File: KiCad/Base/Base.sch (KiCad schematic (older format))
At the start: 27 parts

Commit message: Base board draft 1
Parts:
- removed J?: Conn_01x02_Male, symbol Connector:Conn_01x02_Male
- removed Q?: IRF540N, Package_TO_SOT_THT:TO-220-3_Vertical, symbol Transistor_FET:IRF540N
- removed SW?: Power, symbol Switch:SW_SPDT
- removed U?: 4050, symbol 4xxx:4050
- removed U?: SHT1x, symbol Sensor:SHT1x
- added J14: Power_switch, Connector_PinHeader_2.54mm:PinHeader_1x02_P2.54mm_Vertical, symbol Connector:Conn_01x02_Male
- added J15: VCC, Connector_PinHeader_2.54mm:PinHeader_1x10_P2.54mm_Vertical, symbol Connector:Conn_01x10_Male
- added J16: GND, Connector_PinHeader_2.54mm:PinHeader_1x10_P2.54mm_Vertical, symbol Connector:Conn_01x10_Male
- J1: renamed from J?; footprint (none) -> Connector_PinHeader_2.54mm:PinHeader_2x20_P2.54mm_Vertical
- J10: renamed from J?; value Conn_01x02_Male -> MOSFET_output_1; footprint (none) -> Connector_PinHeader_2.54mm:PinHeader_1x02_P2.54mm_Vertical
- J11: renamed from J?; value Conn_01x02_Male -> MOSFET_output_2; footprint (none) -> Connector_PinHeader_2.54mm:PinHeader_1x02_P2.54mm_Vertical
- J12: renamed from J?; value Conn_01x02_Male -> MOSFET_output_3; footprint (none) -> Connector_PinHeader_2.54mm:PinHeader_1x02_P2.54mm_Vertical
- J2, J3: renamed from J?; footprint (none) -> Connector_PinHeader_2.54mm:PinHeader_1x10_P2.54mm_Vertical
- J4: renamed from J?; footprint (none) -> Connector_BarrelJack:BarrelJack_Horizontal
- J5: renamed from J?; footprint (none) -> Connector_PinHeader_2.54mm:PinHeader_1x04_P2.54mm_Vertical
- J6, J7, J8: renamed from J?; footprint (none) -> Connector_PinHeader_2.54mm:PinHeader_1x14_P2.54mm_Vertical
- J9: renamed from J?; value Conn_01x02_Male -> MOSFET_output_0; footprint (none) -> Connector_PinHeader_2.54mm:PinHeader_1x02_P2.54mm_Vertical
- R1, R2: renamed from R?; footprint (none) -> Resistor_THT:R_Axial_DIN0207_L6.3mm_D2.5mm_P10.16mm_Horizontal
- U1: renamed from U?; footprint (none) -> Package_DIP:DIP-16_W7.62mm_Socket
- gave numbers to parts that had none: 4
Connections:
- net labels added: PWM0
- net labels removed: GPC6, GPC7, GPC8, GPC9, MOUT4
- wire segments 127 -> 162
- no-connect marks 4 -> 8
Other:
- note removed: "CHECK PINS FOR THIS"
- note removed: "Draw in pull-up resistors"
- moved on the sheet: J6, J7, J8

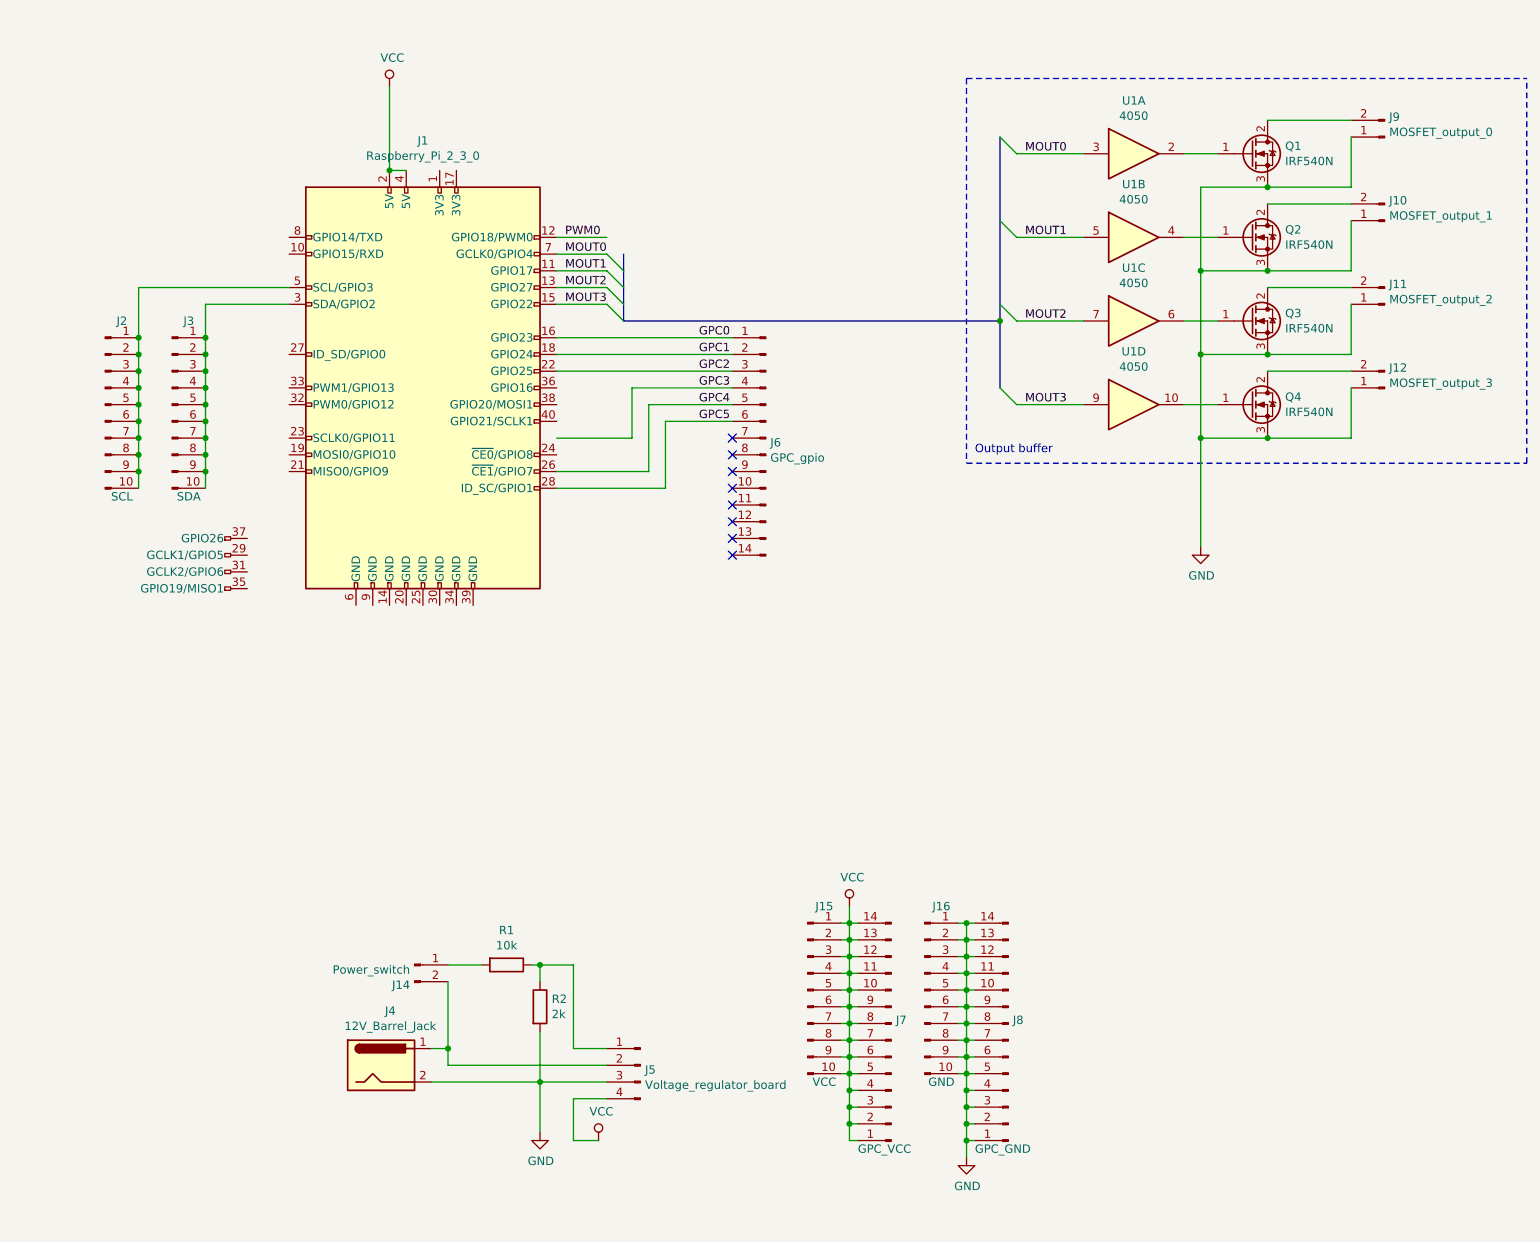
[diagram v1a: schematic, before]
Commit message: Added pull-down resistors to MOSFET outputs
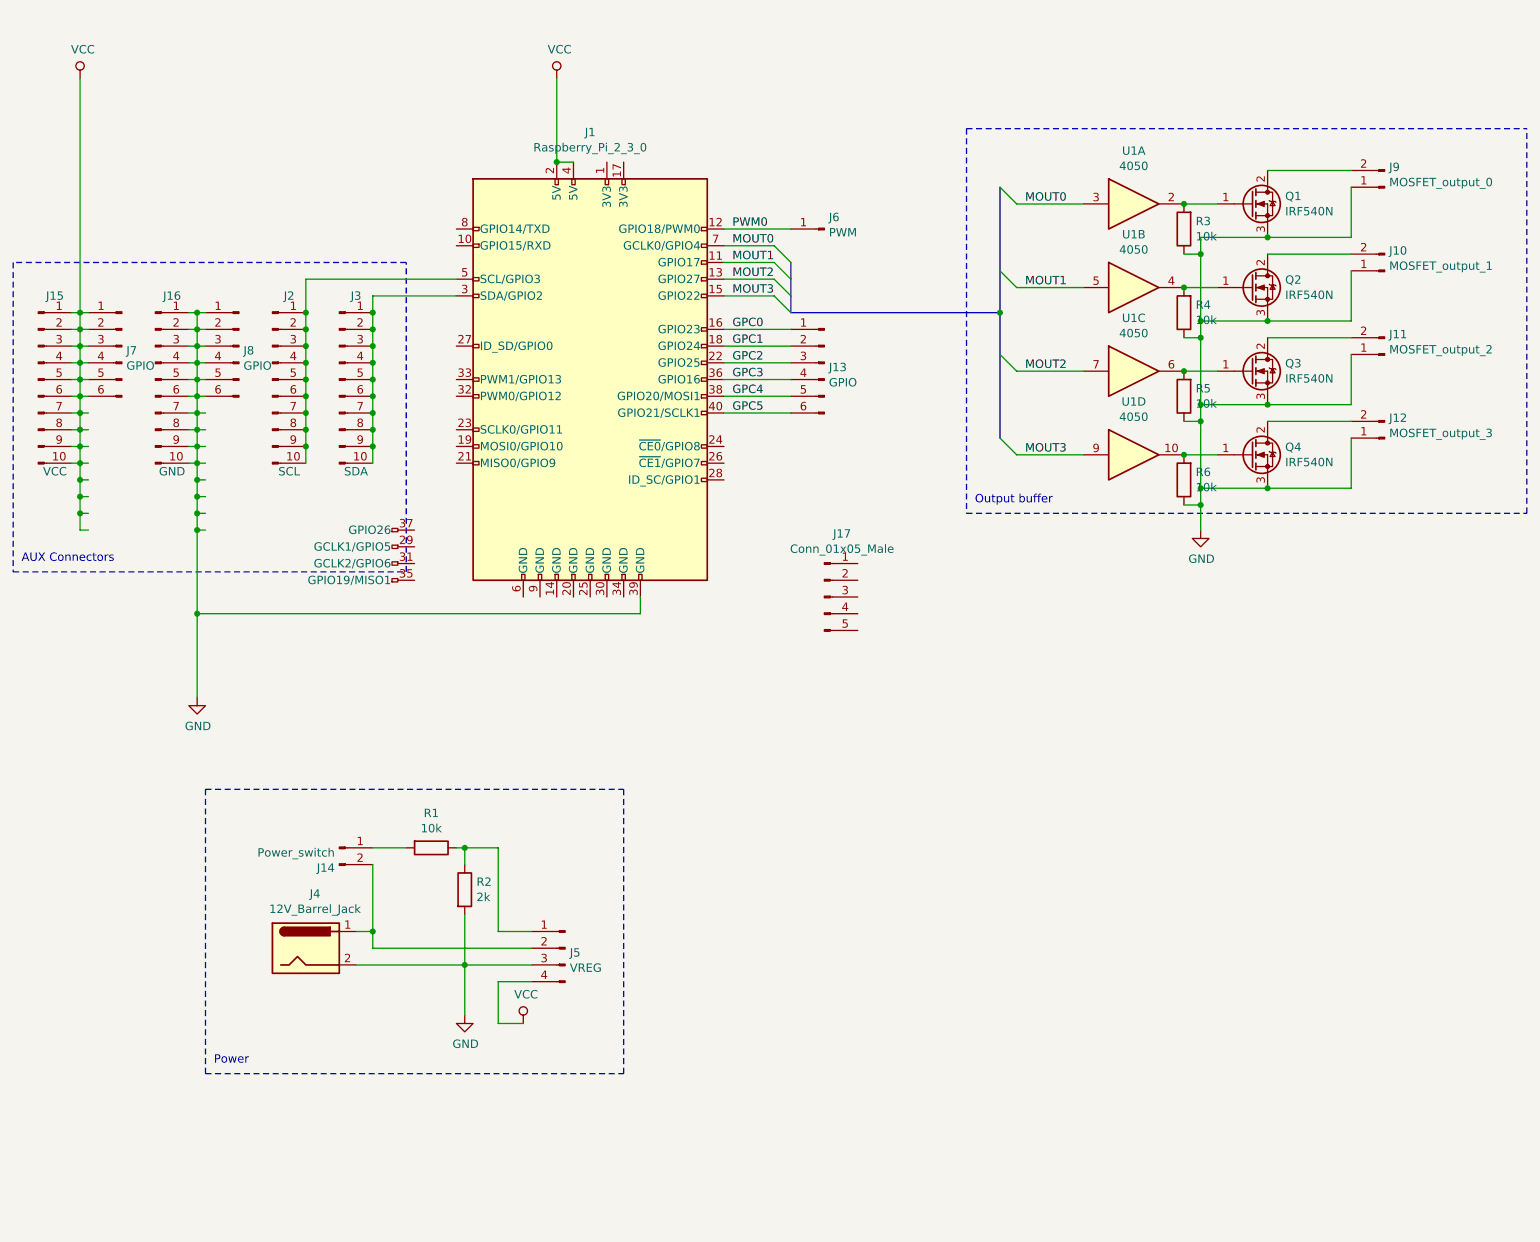
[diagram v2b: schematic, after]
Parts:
- removed J6: GPC_gpio, Connector_PinHeader_2.54mm:PinHeader_1x14_P2.54mm_Vertical, symbol Connector:Conn_01x14_Male
- removed J7: GPC_VCC, Connector_PinHeader_2.54mm:PinHeader_1x14_P2.54mm_Vertical, symbol Connector:Conn_01x14_Male
- removed J8: GPC_GND, Connector_PinHeader_2.54mm:PinHeader_1x14_P2.54mm_Vertical, symbol Connector:Conn_01x14_Male
- added J13, J7, J8: GPIO, Connector_PinHeader_2.54mm:PinHeader_1x06_P2.54mm_Vertical, symbol Connector:Conn_01x06_Male
- added J17: Conn_01x05_Male, symbol Connector:Conn_01x05_Male
- added J6: PWM, Connector_PinHeader_2.54mm:PinHeader_1x01_P2.54mm_Vertical, symbol Connector:Conn_01x01_Male
- added R3, R4, R5, R6: 10k, Resistor_THT:R_Axial_DIN0207_L6.3mm_D2.5mm_P10.16mm_Horizontal, symbol Device:R
- J5: value Voltage_regulator_board -> VREG
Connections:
- wire segments 162 -> 167
- no-connect marks 8 -> 0
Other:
- note added: "AUX Connectors"
- note added: "Power"
- moved on the sheet: J1, J10, J11, J12, J14, J15, J16, J2, J3, J4, J5, J9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

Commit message: Added configurator. Tested base_controller in base_board
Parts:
- removed J17: Conn_01x05_Male, symbol Connector:Conn_01x05_Male
- J1: symbol NewConnector:Raspberry_Pi_2_3_0 -> Base-rescue:Raspberry_Pi_2_3_0-NewConnector
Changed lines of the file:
@@
 Connection ~ 3350 6350
 $Comp
-L NewConnector:Raspberry_Pi_2_3_0 J1
+L Base-rescue:Raspberry_Pi_2_3_0-NewConnector J1
 U 1 1 5BFC5D1D
 P 4100 2850
@@
 	1750 4250 4400 4250
 $Comp
-L Connector:Conn_01x05_Male J17
-U 1 1 5C021A01
-P 5500 4150
-F 0 "J17" H 5606 4528 50  0000 C CNN
-F 1 "Conn_01x05_Male" H 5606 4437 50  0000 C CNN
-F 2 "" H 5500 4150 50  0001 C CNN
-F 3 "~" H 5500 4150 50  0001 C CNN
-	1    5500 4150
-	1    0    0    -1
-$EndComp
-$Comp
 L Device:R R4
 U 1 1 5C0377B8
@@
 Wire Wire Line
 	7650 3100 7750 3100
+Connection ~ 7750 3100
+Wire Wire Line
+	7750 3100 7750 3500
 Wire Bus Line
 	6550 2450 6550 3200
@@
 Wire Bus Line
 	5300 2150 5300 2450
-Connection ~ 7750 3100
-Wire Wire Line
-	7750 3100 7750 3500
 $EndSCHEMATC
